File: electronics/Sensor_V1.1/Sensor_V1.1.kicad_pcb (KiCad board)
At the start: 2 copper layers, 45.9 x 25.6 mm, 44 parts, among them J1 nuclone_small_left, J2 nuclone_small_right, J5 DevBoardUartInput, Q1 DMG1012, Q2 DMG1012, Q3 DMG1012, U1 PPG_sensor, U2 reference_sot23-3, U3 MCP6541

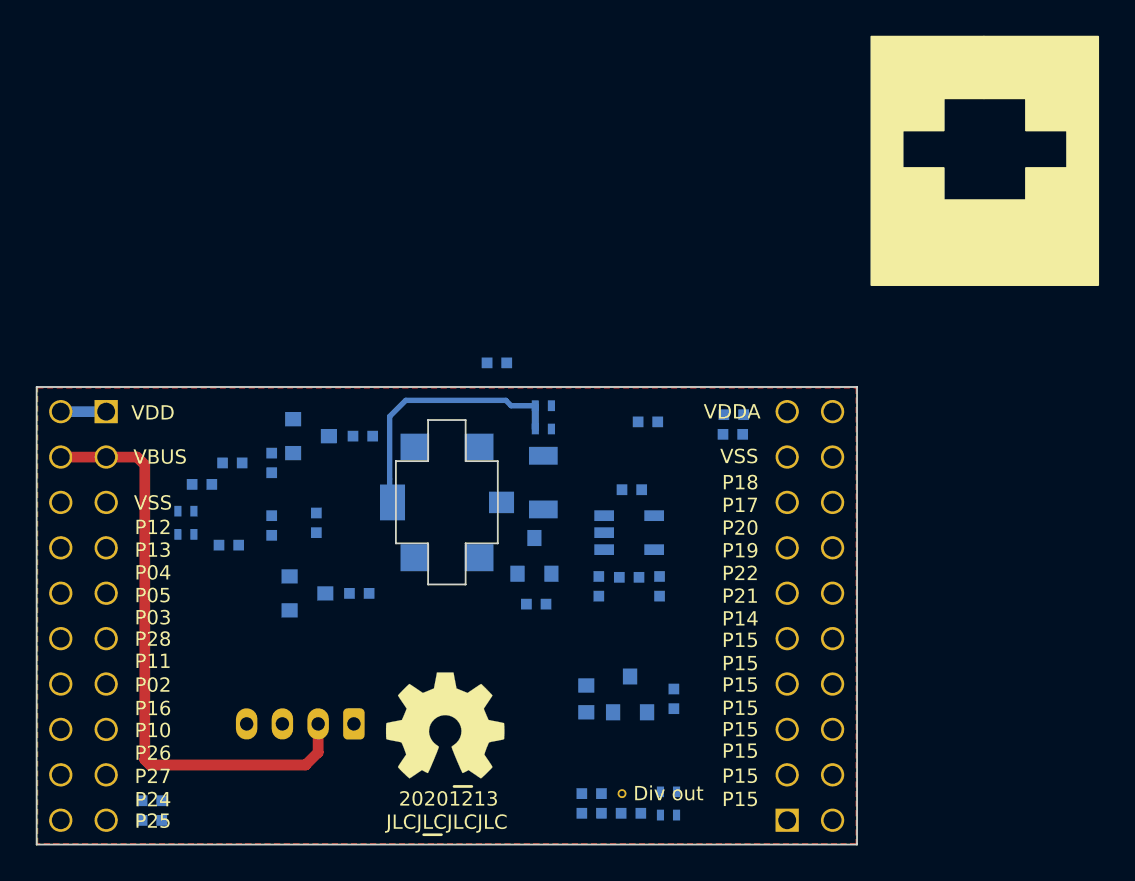
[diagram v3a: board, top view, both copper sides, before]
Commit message: placed LED drive
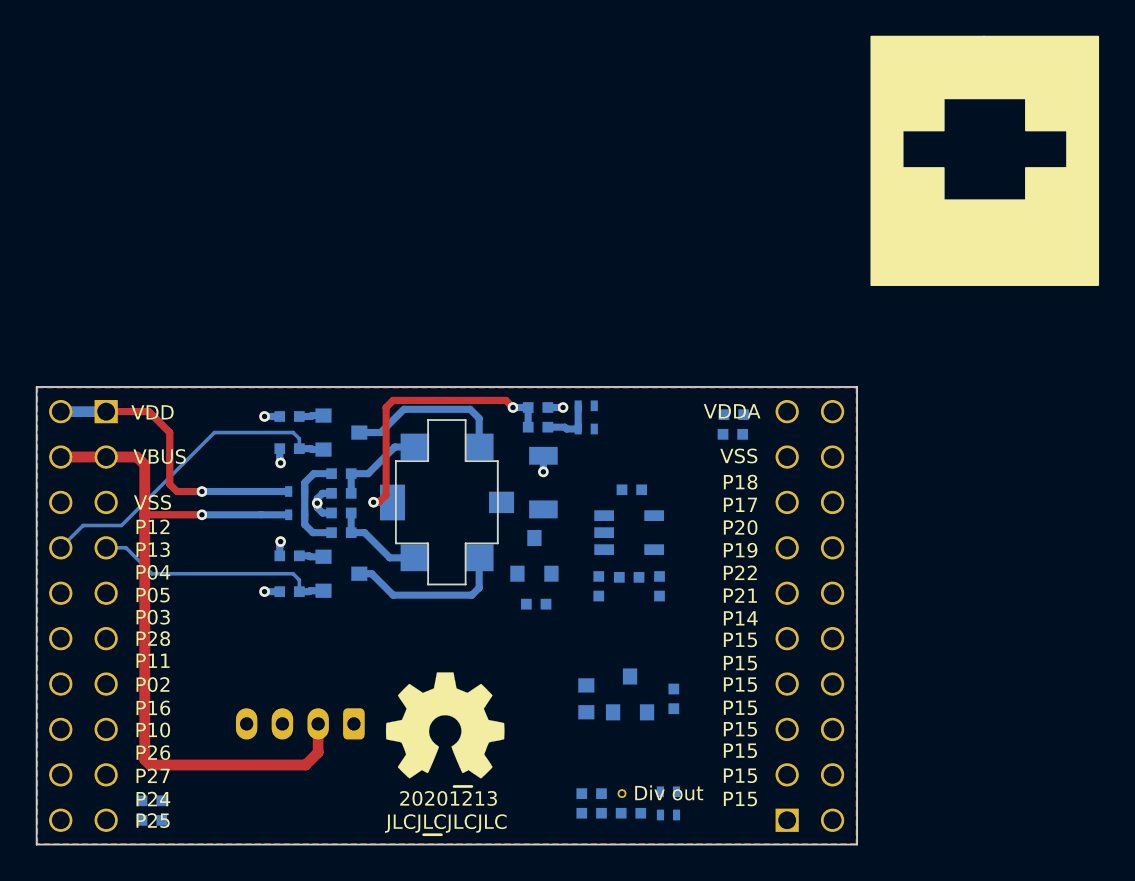
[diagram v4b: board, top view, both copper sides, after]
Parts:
- moved R11 7.82 mm to (79.2, 78.4)
- moved R10 7.24 mm to (79.2, 81.7)
- moved C3 6.94 mm to (79.2, 79.5), turned to 180 degrees
- moved JP2 6.65 mm to (76.7, 79.4)
- moved JP6 6.20 mm to (76.7, 80.7)
- moved FB3 6.16 mm to (90.2, 75.8)
- moved R3 4.43 mm to (76.3, 83.0)
- moved R4 4.24 mm to (76.3, 75.2)
- moved R5 3.83 mm to (76.3, 85.0), turned to 0 degrees
- moved C1 3.40 mm to (90.2, 74.7), turned to 180 degrees
- moved JP1 2.40 mm to (92.9, 74.6)
- moved JP3 2.40 mm to (92.9, 75.9)
- moved Q2 2.20 mm to (79.2, 84.0)
- moved Q3 1.71 mm to (79.2, 76.1)
- moved C2 1.50 mm to (79.2, 80.6), turned to 180 degrees
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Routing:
- net /LED2_EN: track 0.00 -> 18.1 mm
- net /VDD: track 2.54 -> 16.3 mm, vias 0 -> 1
- net /LED1_EN: track 0.00 -> 13.6 mm
- net /LED2_C: track 0.00 -> 9.06 mm
- net /LED1_C: track 0.00 -> 9.06 mm
- net /VBUS: track 33.1 -> 41.1 mm, vias 0 -> 1
- net /VSS: track 0.00 -> 7.44 mm, vias 0 -> 7
- net /LED_VDD: track 0.00 -> 5.74 mm
- net /LED2_A: track 0.00 -> 5.28 mm
- net /LED1_A: track 0.00 -> 5.24 mm
- net Net-(FB3-Pad1): track 0.00 -> 3.04 mm
- net /PD_BIAS: track 14.0 -> 15.9 mm, vias 0 -> 2
- net Net-(Q3-Pad2): track 0.00 -> 1.37 mm
- net Net-(Q2-Pad2): track 0.00 -> 1.37 mm

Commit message: placed more parts on the integrator/comparator side
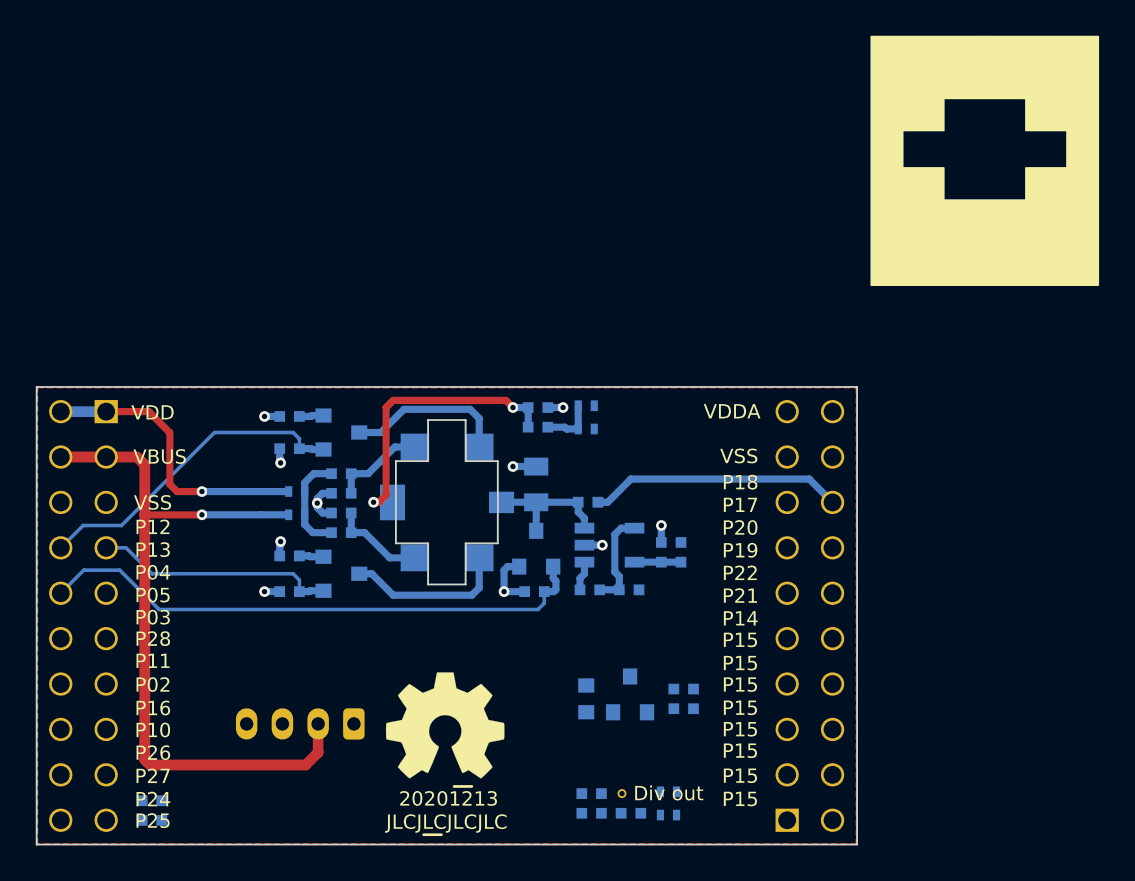
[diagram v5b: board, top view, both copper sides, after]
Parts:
- C9: footprint SquantorRcl:C_1206 -> SquantorRcl:C_0805
- moved FB1 16.1 mm to (98.9, 91.0), turned to 270 degrees
- moved FB2 7.21 mm to (98.2, 82.8), turned to 270 degrees
- moved R9 2.55 mm to (93.0, 80.0)
- moved C10 2.28 mm to (97.1, 82.8), turned to 90 degrees
- moved R18 1.71 mm to (95.3, 84.9), turned to 180 degrees
- moved U3 1.30 mm to (94.2, 82.4)
- moved R8 0.71 mm to (90.0, 85.0)
- moved R17 0.54 mm to (93.1, 84.9), turned to 0 degrees
- moved C9 0.41 mm to (90.1, 79.0)
- moved Q1 0.41 mm to (90.1, 82.6)
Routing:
- net /I_reset: track 0.00 -> 31.3 mm
- net /PD_ADC: track 0.00 -> 14.2 mm
- net /PD_OUT: track 0.00 -> 7.32 mm
- net /VSS: track 7.44 -> 13.1 mm, vias 7 -> 10
- net Net-(R17-Pad2): track 0.00 -> 5.55 mm
- net Net-(C10-Pad1): track 0.00 -> 2.60 mm
- net /CMP_OUT: track 0.00 -> 1.65 mm

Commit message: placed resistor divider and voltage reference
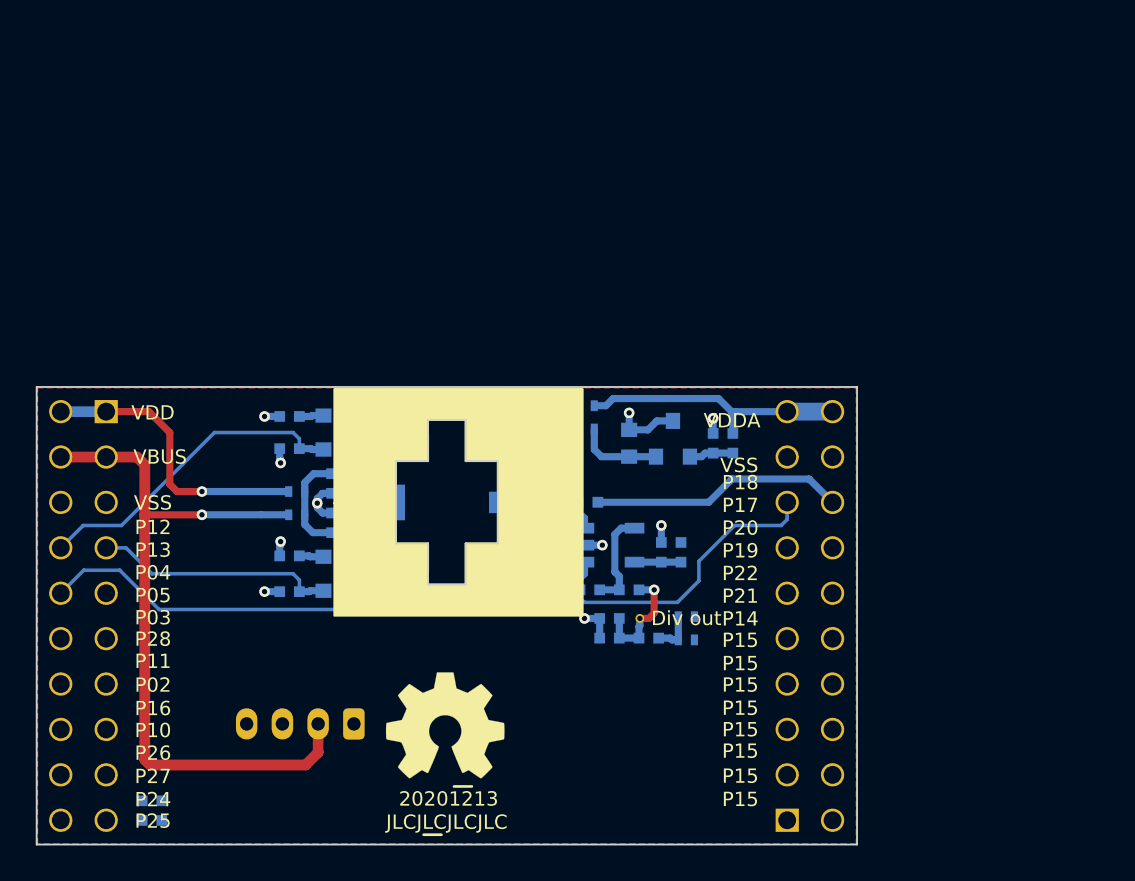
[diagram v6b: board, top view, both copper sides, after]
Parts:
- moved U2 14.5 mm to (97.8, 76.5)
- moved C6 14.5 mm to (95.3, 76.7)
- moved C5 14.5 mm to (100.0, 76.7)
- moved FB1 14.5 mm to (101.1, 76.7)
- moved R12 9.85 mm to (94.2, 87.6)
- moved R7 9.85 mm to (96.4, 87.6)
- moved C11 9.85 mm to (94.2, 86.5)
- moved JP4 9.85 mm to (98.5, 87.7)
- moved JP5 9.85 mm to (98.5, 86.4)
- moved TP11 9.85 mm to (95.9, 86.5)
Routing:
- net /CMP_OUT: track 1.65 -> 17.3 mm
- net /VDDA: track 0.00 -> 15.1 mm
- net /VSS: track 13.1 -> 19.5 mm, vias 10 -> 13
- net /Divider_out: track 0.00 -> 6.39 mm, vias 0 -> 1
- net /VREF: track 0.00 -> 4.77 mm
- net Net-(C5-Pad1): track 0.00 -> 2.48 mm
- net Net-(JP4-Pad2): track 0.00 -> 2.44 mm

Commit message: fixed DRC issues
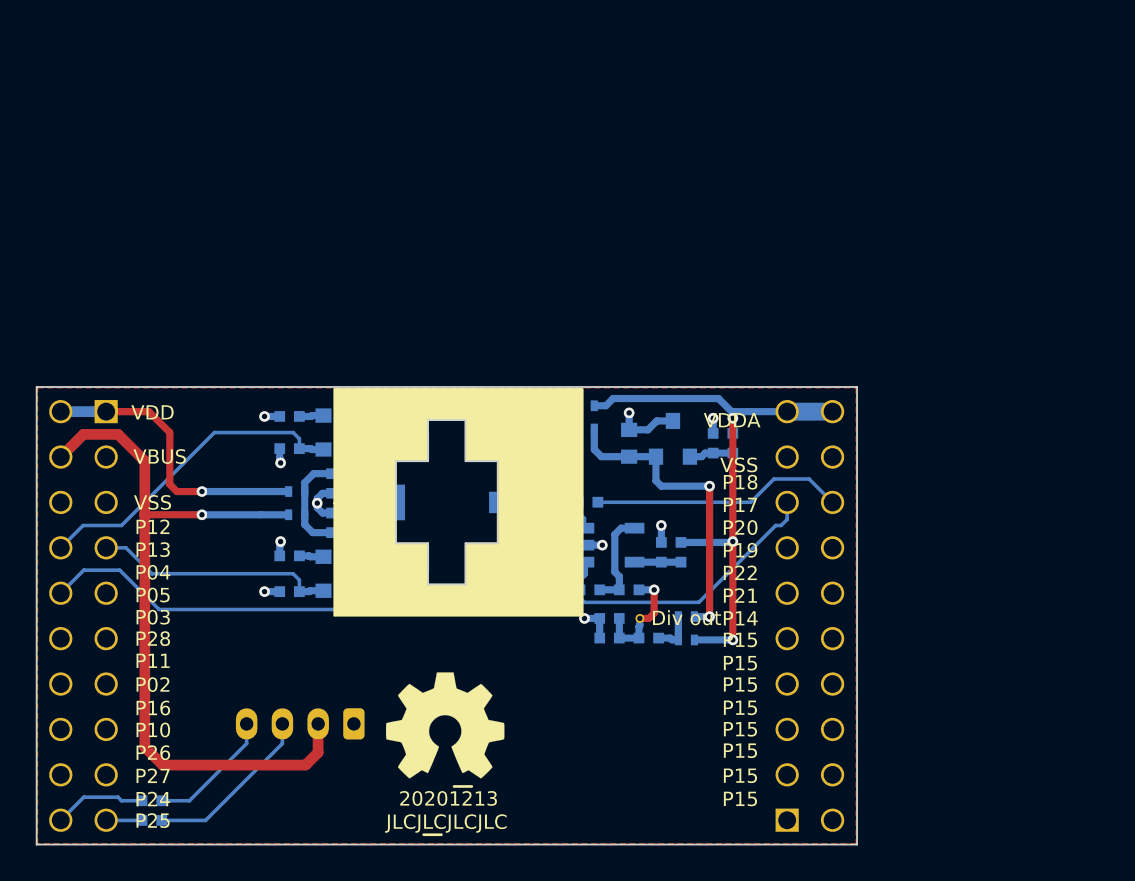
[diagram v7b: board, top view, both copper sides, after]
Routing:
- net /VDDA: track 15.1 -> 32.5 mm, vias 0 -> 3
- net /VREF: track 4.77 -> 17.4 mm, vias 0 -> 2
- net Net-(J5-Pad3): track 0.00 -> 9.63 mm
- net Net-(J5-Pad4): track 0.00 -> 7.18 mm
- net /UART_RX: track 0.00 -> 5.17 mm
- net /UART_TX: track 0.00 -> 2.01 mm
- net /VBUS: track 41.1 -> 41.9 mm
- net /CMP_OUT: track 17.3 -> 16.7 mm
